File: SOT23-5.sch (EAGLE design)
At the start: 14 parts, among them J1 1X03, J2 1X03, J3 1X03, J4 1X03, J5 1X03, J6 1X03, J7 1X03, U1 SOT23-3, U2 SOT23-3, U3 SOT23-3, U4 SOT23-3, U5 SOT23-3, U6 SOT23-3, U7 SOT23-3

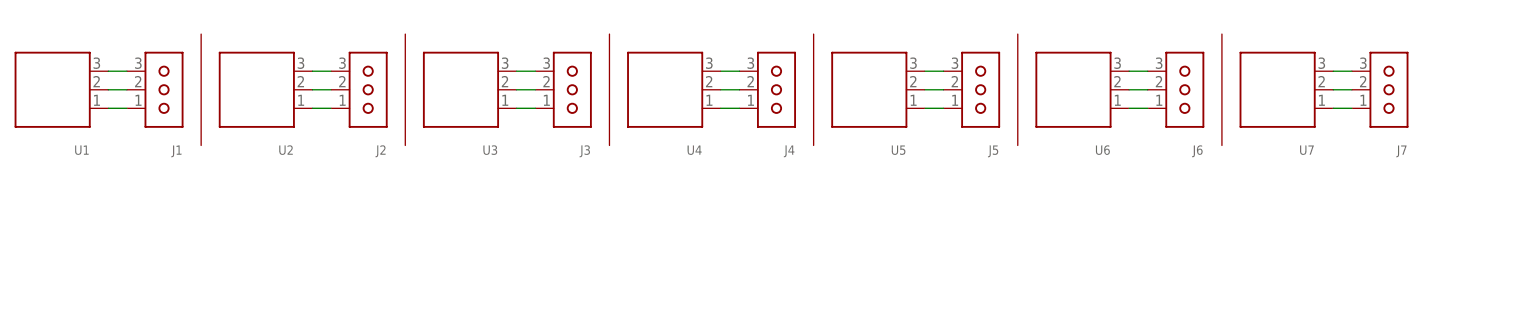
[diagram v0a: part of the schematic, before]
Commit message: Added an SOT23-5 breakout.
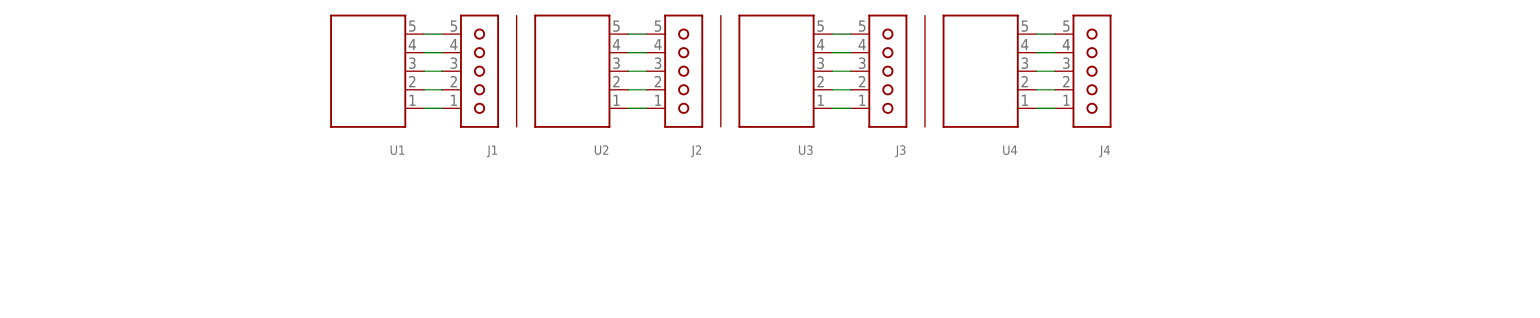
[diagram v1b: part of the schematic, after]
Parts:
- removed J5, J6, J7: 1X03, breakouts:1X03
- removed U5, U6, U7: SOT23-3, breakouts:SOT23-3
- J1, J2, J3, J4: value 1X03 -> 1X05; device breakouts:1X03 -> breakouts:1X05
- U1, U2, U3, U4: value SOT23-3 -> SOT23-5; device breakouts:SOT23-3 -> breakouts:SOT23-5
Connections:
- removed net N$13: J5.1, U5.1
- removed net N$14: J5.2, U5.2
- removed net N$15: J5.3, U5.3
- removed net N$16: J6.1, U6.1
- removed net N$17: J6.2, U6.2
- removed net N$18: J6.3, U6.3
- removed net N$19: J7.1, U7.1
- removed net N$20: J7.2, U7.2
- removed net N$21: J7.3, U7.3
- new net N$22: J1.4, U1.4
- new net N$23: J1.5, U1.5
- new net N$24: J2.4, U2.4
- new net N$25: J2.5, U2.5
- new net N$26: J3.4, U3.4
- new net N$27: J3.5, U3.5
- new net N$28: J4.4, U4.4
- new net N$29: J4.5, U4.5

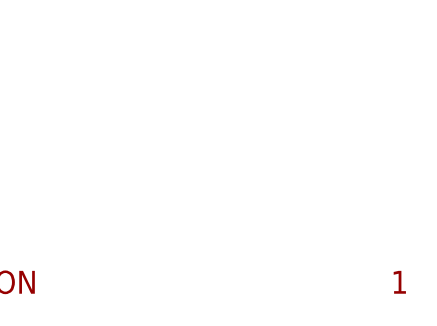
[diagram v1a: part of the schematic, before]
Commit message: Fix some silk screen flaws in pin header devices.
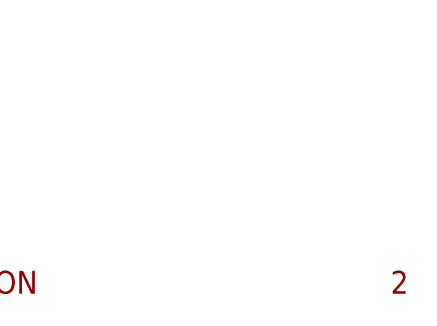
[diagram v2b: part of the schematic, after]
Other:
- note added: "2"
- note removed: "1"
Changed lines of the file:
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@@
 <setting verticaltext="up"/>
 </settings>
-<grid distance="0.1" unitdist="inch" unit="inch" style="lines" multiple="1" display="yes" altdistance="0.01" altunitdist="inch" altunit="inch"/>
+<grid distance="0.1" unitdist="inch" unit="inch" style="lines" multiple="1" display="no" altdistance="0.01" altunitdist="inch" altunit="inch"/>
 <layers>
 <layer number="1" name="Top" color="4" fill="1" visible="no" active="no"/>
@@
 <wire x1="152.4" y1="106.68" x2="152.4" y2="91.44" width="0.1524" layer="94"/>
 <text x="172.72" y="6.35" size="2.54" layer="94">ALAN JOHNSON</text>
-<text x="236.22" y="6.35" size="2.54" layer="94">1</text>
+<text x="236.22" y="6.35" size="2.54" layer="94">2</text>
 </plain>
 <instances>
